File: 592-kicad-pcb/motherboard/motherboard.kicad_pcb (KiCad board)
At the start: 4 copper layers, 151 parts, among them J1 U.FL, J10 Conn_02x06_Odd_Even, J11 Conn_02x06_Odd_Even, J12 Conn_02x06_Odd_Even, J13 Conn_02x06_Odd_Even, J14 USB_B_Micro, J15 Micro_SD_Card, J16 Conn_02x01, J17 Conn_02x01, J18 Conn_02x01, J19 Conn_01x16, J2 U.FL, J20 Conn_02x06_Odd_Even, J21 Conn_02x01, J22 Conn_02x01, J23 Conn_01x16, J24 DF40C-40DP-0.4V(51), J3 DF40C-40DP-0.4V(51), J4 Conn_01x16, J5 2.54mm jumper, J6 U.FL, J7 Conn_02x06_Odd_Even, J8 Conn_02x06_Odd_Even, J9 Conn_02x06_Odd_Even, SW1 C318884, U1 OPA2328DGKR, U10 FT4232H, U11 74HC595, U12 W25Q32JVSS, U13 SN74LVC1G3157DBVR, U14 74CBTLV3257, U15 74CBTLV3257, U16 NUCLEO144-H743ZI, U17 74CBTLV3257, U18 SN74LVC1G14DBV, U19 SN74LVC1G14DBV, U2 74LVC1T45GW, U3 SN74LVC1G14DBV, U4 74LVC1T45GW, U5 SMXS-04K, U6 SX3M10.000B10F20TNN, U7 74LVC1T45GW, U8 SN74LVC1G3157DBVR, U9 SN74LVC1G3157DBVR, Y1 NX3225GA-25.000M-STD-CRG-2, Y2 Si5351A, Y3 X322512MSB4SI

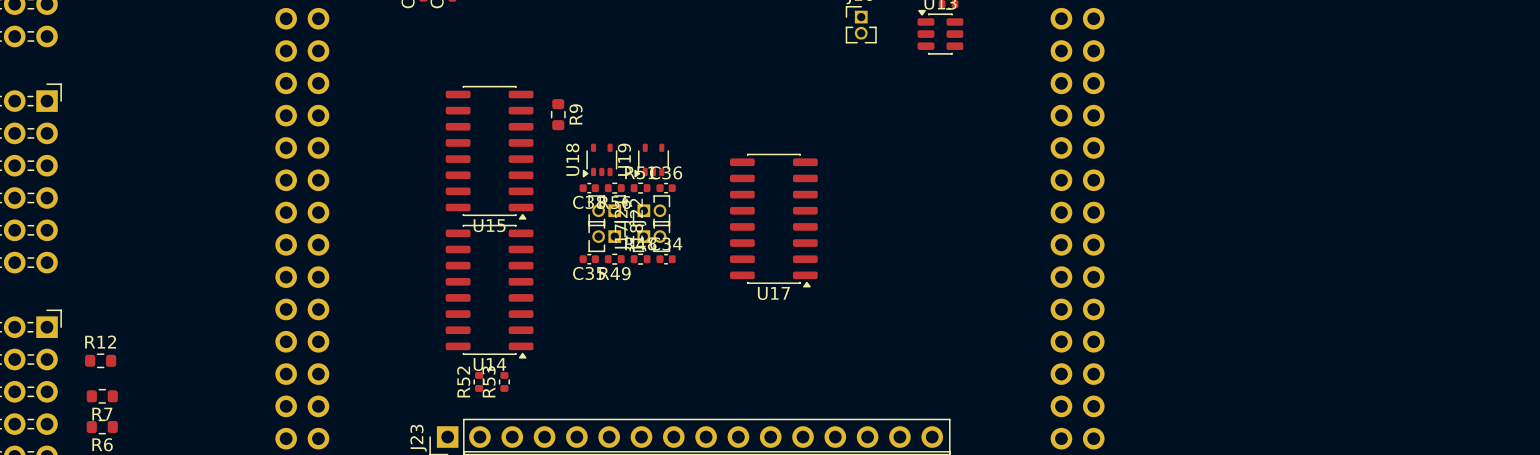
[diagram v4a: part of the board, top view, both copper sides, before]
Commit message: map to STM pins
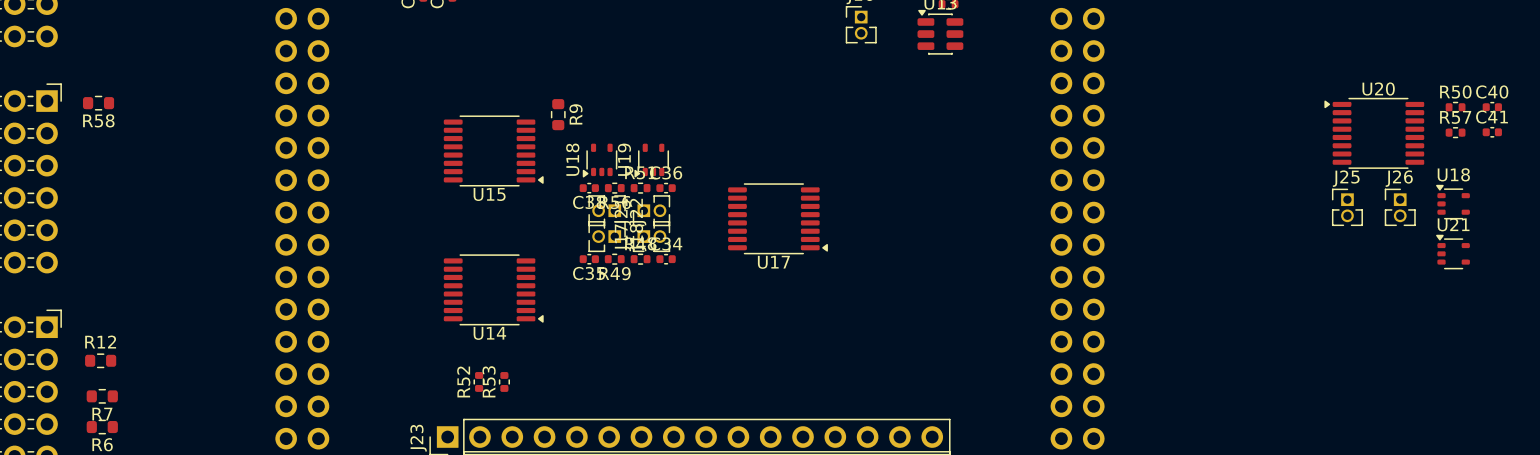
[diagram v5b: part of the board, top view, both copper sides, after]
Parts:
- added C40: 100n, Capacitor_SMD:C_0402_1005Metric, F.Cu at (215.1, 65.8)
- added C41: 100n, Capacitor_SMD:C_0402_1005Metric, F.Cu at (215.1, 67.8)
- added J25: Conn_02x01, Connector_PinHeader_1.27mm:PinHeader_1x02_P1.27mm_Vertical, F.Cu at (203.7, 73.1)
- added J26: Conn_02x01, Connector_PinHeader_1.27mm:PinHeader_1x02_P1.27mm_Vertical, F.Cu at (207.8, 73.1)
- added R50: 10k, Resistor_SMD:R_0402_1005Metric, F.Cu at (212.2, 65.8)
- added R57: 10k, Resistor_SMD:R_0402_1005Metric, F.Cu at (212.2, 67.8)
- added R58: 10k, Resistor_SMD:R_0603_1608Metric, F.Cu at (105.5, 65.5)
- added U18: SN74LVC1G00DCK, Package_TO_SOT_SMD:SOT-353_SC-70-5, F.Cu at (212.1, 73.4)
- added U20: 74CBTLV3257PW,118, Package_SO:TSSOP-16_4.4x5mm_P0.65mm, F.Cu at (206.1, 67.9)
- added U21: SN74LVC1G14DBV, Package_TO_SOT_SMD:SOT-353_SC-70-5, F.Cu at (212.1, 77.3)
- U14, U15, U17: value 74CBTLV3257 -> 74CBTLV3257PW,118; footprint Package_SO:SOIC-16_3.9x9.9mm_P1.27mm -> Package_SO:TSSOP-16_4.4x5mm_P0.65mm

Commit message: updates to routing
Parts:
- added JP3: SolderJumper_2_Bridged, Jumper:SolderJumper-2_P1.3mm_Bridged2Bar_Pad1.0x1.5mm, F.Cu at (-159.7, 59.6)
- added JP4: SolderJumper_2_Bridged, Jumper:SolderJumper-2_P1.3mm_Bridged2Bar_Pad1.0x1.5mm, F.Cu at (-159.7, 63.2)
- added JP5: SolderJumper_2_Bridged, Jumper:SolderJumper-2_P1.3mm_Bridged2Bar_Pad1.0x1.5mm, F.Cu at (-159.7, 66.7)
- moved C14 203.0 mm to (-71.7, 36.4)
- moved C15 203.0 mm to (-66.2, 40.3)
- moved C16 203.0 mm to (-68.1, 40.3)
- moved C18 203.0 mm to (-71.0, 40.6)
- moved C20 203.0 mm to (-73.8, 35.0)
- moved R38 203.0 mm to (-73.8, 33.7)
- moved C19 203.0 mm to (-63.1, 53.5)
- moved C30 203.0 mm to (-59.4, 53.0)
- moved C38 203.0 mm to (12.1, 67.5)
- moved C40 203.0 mm to (12.1, 65.6)
- moved D1 203.0 mm to (-48.2, 53.6)
- moved D2 203.0 mm to (-48.2, 49.8)
- moved D3 203.0 mm to (-48.2, 46.0)
- moved D4 203.0 mm to (-48.2, 42.2)
- moved D5 203.0 mm to (-46.6, 53.6)
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- renumbered C9 to C10, C37 to C11, C10 to C12, C11 to C13, C12 to C14, C13 to C15, C14 to C16, C15 to C17, C16 to C18, C17 to C19, C18 to C20, C19 to C21, C20 to C22, C21 to C23, C22 to C24, C23 to C25, C24 to C26, C25 to C27, C26 to C28, C27 to C29, C28 to C30, C29 to C31, C30 to C32, C31 to C33, C32 to C34, C33 to C35, C38 to C37, C41 to C38, C34 to C39, C35 to C41, C39 to C6, C6 to C7, C7 to C8, C8 to C9, J7 to J10, J8 to J11, J9 to J12, J10 to J13, J11 to J14, J20 to J15, J12 to J16, J13 to J17, J14 to J18, J15 to J19, J16 to J20, J26 to J23, J17 to J24, J18 to J26, J24 to J4, J4 to J5, J19 to J6, J23 to J7, J5 to J8, J6 to J9, R58 to R10, R10 to R11, R11 to R12, R12 to R13, R13 to R14, R14 to R15, R15 to R16, R16 to R17, R17 to R18, R18 to R19, R19 to R20, R20 to R21, R21 to R22, R22 to R23, R23 to R24, R24 to R25, R25 to R26, R26 to R27, R27 to R28, R28 to R29, R29 to R30, R30 to R31, R31 to R32, R32 to R33, R33 to R34, R34 to R35, R35 to R36, R36 to R37, R37 to R38, R38 to R39, R39 to R40, R40 to R41, R41 to R42, R42 to R43, R43 to R44, R44 to R45, R45 to R46, R46 to R47, R54 to R48, R55 to R49, R47 to R50, R56 to R52, R57 to R53, R49 to R54, R48 to R55, R50 to R56, R52 to R57, R53 to R58, U16 to U1, U9 to U10, U10 to U11, U11 to U12, U12 to U13, U13 to U14, U19 to U15, U18 to U16, U14 to U17, U21 to U18, U17 to U19, U1 to U2, U15 to U20, U20 to U21, U2 to U3, U3 to U4, U4 to U5, U5 to U6, U6 to U7, U7 to U8, U8 to U9
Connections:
- J12 pad 2: /motherboard_top/mgmt_debug -> /PG12
- J12 pad 6: /motherboard_top/UART_mgmt_uart_tx -> /PE0_UART8_RX
- J12 pad 8: /motherboard_top/UART_mgmt_uart_rx -> /PE1_UART8_TX
- J3 pad 13: /motherboard_top/chip_connection/user_3v3 -> GND
- J3 pad 2: GND -> /motherboard_top/chip_connection/user_3v3
- J5 pad 1: /motherboard_top/mgmt_debug -> unconnected-(J5-Pin_1-Pad1)
- J5 pad 10: /motherboard_top/chip_connection/MGMT_flash2_sck -> /PE0_UART8_RX
- J5 pad 11: /motherboard_top/chip_connection/MGMT_flash2_io0 -> /PE1_UART8_TX
- J5 pad 12: /motherboard_top/chip_connection/MGMT_flash2_io1 -> /motherboard_top/mgmt_sck
- J5 pad 13: /motherboard_top/chip_connection/MGMT_irq2 -> /motherboard_top/mgmt_csb
- J5 pad 14: unconnected-(J4-Pin_14-Pad14) -> /motherboard_top/mgmt_sdi
- J5 pad 15: unconnected-(J4-Pin_15-Pad15) -> /motherboard_top/mgmt_sdo
- J5 pad 16: unconnected-(J4-Pin_16-Pad16) -> /PG12
- J5 pad 2: /motherboard_top/mgmt_sdo -> unconnected-(J5-Pin_2-Pad2)
- J5 pad 3: /motherboard_top/mgmt_sdi -> unconnected-(J5-Pin_3-Pad3)
- J5 pad 4: /motherboard_top/mgmt_csb -> /PD7
- J5 pad 5: /motherboard_top/mgmt_sck -> /PG1
- J5 pad 6: /motherboard_top/UART_mgmt_uart_rx -> /PG0
- J5 pad 7: /motherboard_top/UART_mgmt_uart_tx -> /PG9
- J5 pad 8: /motherboard_top/chip_connection/MGMT_irq -> /PG15
- J5 pad 9: /motherboard_top/chip_connection/MGMT_flash2_csb -> /PG10
- J6 pad 1: /motherboard_top/chip_connection/mprj_io_0 -> unconnected-(J6-Pin_1-Pad1)
- J6 pad 10: /motherboard_top/chip_connection/mprj_io_9 -> /motherboard_top/chip_connection/mprj_io_6
- J6 pad 11: /motherboard_top/chip_connection/mprj_io_10 -> /motherboard_top/chip_connection/mprj_io_5
- J6 pad 12: /motherboard_top/chip_connection/mprj_io_11 -> /motherboard_top/chip_connection/mprj_io_4
- J6 pad 13: /motherboard_top/chip_connection/mprj_io_12 -> /motherboard_top/chip_connection/mprj_io_3
- J6 pad 14: unconnected-(J19-Pin_14-Pad14) -> /motherboard_top/chip_connection/mprj_io_2
- J6 pad 15: unconnected-(J19-Pin_15-Pad15) -> /motherboard_top/chip_connection/mprj_io_1
- J6 pad 16: unconnected-(J19-Pin_16-Pad16) -> /motherboard_top/chip_connection/mprj_io_0
- J6 pad 2: /motherboard_top/chip_connection/mprj_io_1 -> unconnected-(J6-Pin_2-Pad2)
- J6 pad 3: /motherboard_top/chip_connection/mprj_io_2 -> unconnected-(J6-Pin_3-Pad3)
- J6 pad 4: /motherboard_top/chip_connection/mprj_io_3 -> /motherboard_top/chip_connection/mprj_io_12
- J6 pad 5: /motherboard_top/chip_connection/mprj_io_4 -> /motherboard_top/chip_connection/mprj_io_11
- J6 pad 6: /motherboard_top/chip_connection/mprj_io_5 -> /motherboard_top/chip_connection/mprj_io_10
- J6 pad 7: /motherboard_top/chip_connection/mprj_io_6 -> /motherboard_top/chip_connection/mprj_io_9
- J6 pad 8: /motherboard_top/chip_connection/mprj_io_7 -> /motherboard_top/chip_connection/mprj_io_8
- J6 pad 9: /motherboard_top/chip_connection/mprj_io_8 -> /motherboard_top/chip_connection/mprj_io_7
- J7 pad 1: /motherboard_top/chip_rck_jtag_tck -> unconnected-(J7-Pin_1-Pad1)
- J7 pad 10: /motherboard_top/chip_rck_gpio_0_0 -> /motherboard_top/chip_rck_spi_0_cs_0
- J7 pad 11: /motherboard_top/chip_rck_gpio_1_0 -> /motherboard_top/chip_rck_spi_0_dq_0_mosi
- J7 pad 12: /motherboard_top/chip_rck_i2c_sda -> /motherboard_top/chip_rck_spi_0_dq_1_miso
- J7 pad 13: /motherboard_top/chip_rck_i2c_scl -> /motherboard_top/chip_rck_jtag_tdo
- J7 pad 14: unconnected-(J23-Pin_14-Pad14) -> /motherboard_top/chip_rck_jtag_tdi
- J7 pad 15: unconnected-(J23-Pin_15-Pad15) -> /motherboard_top/chip_rck_jtag_tms
- J7 pad 16: unconnected-(J23-Pin_16-Pad16) -> /motherboard_top/chip_rck_jtag_tck
- J7 pad 2: /motherboard_top/chip_rck_jtag_tms -> unconnected-(J7-Pin_2-Pad2)
- J7 pad 3: /motherboard_top/chip_rck_jtag_tdi -> unconnected-(J7-Pin_3-Pad3)
- J7 pad 4: /motherboard_top/chip_rck_jtag_tdo -> /motherboard_top/chip_rck_i2c_scl
- J7 pad 5: /motherboard_top/chip_rck_spi_0_dq_1_miso -> /motherboard_top/chip_rck_i2c_sda
- J7 pad 6: /motherboard_top/chip_rck_spi_0_dq_0_mosi -> /motherboard_top/chip_rck_gpio_1_0
- J7 pad 7: /motherboard_top/chip_rck_spi_0_cs_0 -> /motherboard_top/chip_rck_gpio_0_0
- J7 pad 8: /motherboard_top/chip_rck_spi_0_sck -> /motherboard_top/GPIO_chip_rck_reset_io
- J7 pad 9: /motherboard_top/GPIO_chip_rck_reset_io -> /motherboard_top/chip_rck_spi_0_sck
- J8 pad 3: /motherboard_top/chip_support_misc/VREF_DAC_OUT -> /PA4_DAC_OUT1
- R25 pad 2: /motherboard_top/clock_sources/fs_ext_gen -> /motherboard_top/clock_sources/ext_clk_dig_gen
- R26 pad 2: /motherboard_top/clock_sources/ext_clk_dig_gen -> /motherboard_top/clock_sources/fs_ext_gen
- R29 pad 2: /motherboard_top/clock_sources/ext_clk_dig_gen -> /motherboard_top/clock_sources/fs_ext_gen
- R31 pad 2: /motherboard_top/clock_sources/fs_ext_gen -> /motherboard_top/clock_sources/ext_clk_dig_gen
- R34 pad 2: /motherboard_top/clock_sources/CLK_DIG_GPIO_GEN -> /PB14_TIM12_CH1
- U1 pad 100: unconnected-(U16-LD3/PB14-Pad100) -> /PB14_TIM12_CH1
- U1 pad 11: unconnected-(U16-PF7-Pad11) -> /PF7_SPI5_SCK
- U1 pad 136: unconnected-(U16-PE0-Pad136) -> /PE0_UART8_RX
- U1 pad 28: unconnected-(U16-PA0-Pad28) -> /PA0_UART4_RX
- U1 pad 30: unconnected-(U16-ETH_REF_CLK/PA1-Pad30) -> /PA1_UART4_TX
- U1 pad 32: unconnected-(U16-PA4-Pad32) -> /PA4_DAC_OUT1
- U1 pad 45: unconnected-(U16-PD7-Pad45) -> /PD7
- U1 pad 54: unconnected-(U16-PF8-Pad54) -> /PF8_SPI5_MISO
- U1 pad 56: unconnected-(U16-PF9-Pad56) -> /PF9_SPI5_MOSI
- U1 pad 58: unconnected-(U16-PG1-Pad58) -> /PG1
- U1 pad 59: unconnected-(U16-PG0-Pad59) -> /PG0
- U1 pad 61: unconnected-(U16-PE1-Pad61) -> /PE1_UART8_TX
- U1 pad 63: unconnected-(U16-PG9-Pad63) -> /PG9
- U1 pad 64: unconnected-(U16-PG15-Pad64) -> /PG15
- U1 pad 65: unconnected-(U16-PG12-Pad65) -> /PG12
- U1 pad 66: unconnected-(U16-PG10-Pad66) -> /PG10
- U1 pad 75: unconnected-(U16-PB8-Pad75) -> /PB8_I2C4_SCL
- U1 pad 77: unconnected-(U16-PB9-Pad77) -> /PB9_I2C4_SDA
- U1 pad 9: unconnected-(U16-PF6-Pad9) -> /PF6_SPI5_CS
- U10 pad 3: /motherboard_top/clock_sources/CLK_DIG_GPIO_GEN -> /PB14_TIM12_CH1
- U11 pad 38: /motherboard_top/UART_mgmt_uart_rx -> /PE1_UART8_TX
- U11 pad 39: /motherboard_top/UART_mgmt_uart_tx -> /PE0_UART8_RX
- U11 pad 48: /motherboard_top/ftdi/ftdi4_uart_tx -> /PA0_UART4_RX
- U11 pad 52: /motherboard_top/ftdi/ftdi4_uart_rx -> /PA1_UART4_TX
- U18 pad 1: unconnected-(U21-NC-Pad1) -> unconnected-(U18-NC-Pad1)
- U19 pad 10: /motherboard_top/GPIO_chip_nfc_jtag_tdo -> /motherboard_top/chip_nfc_jtag_tms
- U19 pad 11: /motherboard_top/chip_rck_jtag_tdo -> /motherboard_top/chip_rck_jtag_tms
- U19 pad 2: /motherboard_top/chip_rck_jtag_tms -> /motherboard_top/chip_rck_jtag_tdo
- U19 pad 3: /motherboard_top/chip_nfc_jtag_tms -> /motherboard_top/GPIO_chip_nfc_jtag_tdo
- U19 pad 4: /motherboard_top/ftdi1_jtag_tms -> /motherboard_top/ftdi1_jtag_tdo
- U19 pad 9: /motherboard_top/ftdi1_jtag_tdo -> /motherboard_top/ftdi1_jtag_tms
- U21 pad 10: /motherboard_top/SPI_MGMT_MOSI -> /PF9_SPI5_MOSI
- U21 pad 13: /motherboard_top/SPI_MGMT_MISO -> /PF8_SPI5_MISO
- U21 pad 3: /motherboard_top/SPI_MGMT_CSb -> /PF6_SPI5_CS
- U21 pad 6: /motherboard_top/SPI_MGMT_SCK -> /PF7_SPI5_SCK
- Y2 pad 4: /motherboard_top/clock_sources/SCL -> /PB8_I2C4_SCL
- Y2 pad 5: /motherboard_top/clock_sources/SDA -> /PB9_I2C4_SDA
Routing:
- net /motherboard_top/chip_nfc_fs: track 0.00 -> 27.2 mm
- net /motherboard_top/chip_nfc_ana_mux_out_2: track 0.00 -> 22.1 mm, vias 0 -> 2
- net /motherboard_top/chip_nfc_ext_clk_dig: track 0.00 -> 18.7 mm
- net +3V3: track 0.00 -> 11.2 mm
- net /motherboard_top/chip_rck_jtag_tdo: track 0.00 -> 9.50 mm
- net GND: track 0.00 -> 9.30 mm, vias 0 -> 2
- net /motherboard_top/chip_rck_jtag_tck: track 0.00 -> 8.85 mm
- net /motherboard_top/chip_rck_jtag_tdi: track 0.00 -> 8.33 mm
- net /motherboard_top/chip_rck_jtag_tms: track 0.00 -> 7.83 mm
- net /PB14_TIM12_CH1: track 0.00 -> 7.71 mm
- net +1V8: track 0.00 -> 6.48 mm
- net Net-(Y2-XA): track 0.00 -> 6.23 mm
- net Net-(Y2-XB): track 0.00 -> 6.23 mm
- net /motherboard_top/clock_sources/EXT_CLK_DIG_SEL: track 0.00 -> 5.08 mm
- net /motherboard_top/clock_sources/CARAVEL_CLK_EN: track 0.00 -> 5.03 mm
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
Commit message: more routing progress, add termination resistors
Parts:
- moved R1 275.4 mm to (176.7, 108.6)
- moved U3 275.3 mm to (174.4, 109.2)
- moved R23 13.1 mm to (188.0, 105.5), turned to 180 degrees
- moved C8 12.4 mm to (188.0, 104.4), turned to 0 degrees
- moved R24 11.7 mm to (188.0, 103.0), turned to 180 degrees
- moved C10 11.3 mm to (188.0, 101.9), turned to 0 degrees
- moved C12 11.3 mm to (188.0, 99.4), turned to 0 degrees
- moved R30 11.2 mm to (188.0, 100.5), turned to 180 degrees
- moved U6 1.62 mm to (194.9, 101.2), turned to 90 degrees
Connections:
- C10 pad 2: /motherboard_top/clock_sources/CARAVEL_CLK_EN -> /motherboard_top/clock_sources/FS_EXT_SEL
- C12 pad 2: /motherboard_top/clock_sources/FS_EXT_SEL -> /motherboard_top/clock_sources/CARAVEL_CLK_EN
- R24 pad 1: /motherboard_top/clock_sources/CARAVEL_CLK_EN -> /motherboard_top/clock_sources/FS_EXT_SEL
- R30 pad 1: /motherboard_top/clock_sources/FS_EXT_SEL -> /motherboard_top/clock_sources/CARAVEL_CLK_EN
- U6 pad 6: /motherboard_top/clock_sources/FS_EXT_SEL -> /motherboard_top/clock_sources/CARAVEL_CLK_EN
- U6 pad 7: /motherboard_top/clock_sources/CARAVEL_CLK_EN -> /motherboard_top/clock_sources/FS_EXT_SEL
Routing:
- net /motherboard_top/chip_rck_clock_uncore: track 4.40 -> 34.2 mm
- net /motherboard_top/chip_nfc_ana_mux_out: track 0.00 -> 24.0 mm, vias 0 -> 2
- net /motherboard_top/clock_sources/FS_EXT_SEL: track 5.01 -> 27.6 mm, vias 0 -> 2
- net /motherboard_top/clock_sources/CARAVEL_CLK_EN: track 5.03 -> 24.9 mm
- net /motherboard_top/clock_sources/EXT_CLK_DIG_SEL: track 5.08 -> 22.8 mm, vias 0 -> 2
- net /motherboard_top/chip_nfc_nfc_afe_tdo: track 1.06 -> 6.32 mm
- net /motherboard_top/chip_connection/user_3v3: track 0.00 -> 3.39 mm, vias 0 -> 2
- net /motherboard_top/chip_connection/mprj_io_7: track 0.00 -> 2.72 mm, vias 0 -> 1
- net /motherboard_top/chip_connection/mprj_io_12: track 0.00 -> 2.44 mm, vias 0 -> 1
- net /motherboard_top/chip_connection/mprj_io_6: track 0.00 -> 2.31 mm, vias 0 -> 1
- net /motherboard_top/chip_connection/mprj_io_8: track 0.00 -> 2.20 mm, vias 0 -> 1
- net /motherboard_top/chip_connection/mprj_io_11: track 0.00 -> 2.19 mm, vias 0 -> 1
- net /motherboard_top/GPIO_chip_nfc_jtag_tdo2: track 0.00 -> 1.87 mm, vias 0 -> 1
- net /motherboard_top/chip_connection/mprj_io_5: track 0.00 -> 1.81 mm, vias 0 -> 1
- net /motherboard_top/chip_connection/mprj_io_9: track 0.00 -> 1.77 mm, vias 0 -> 1
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
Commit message: core routing progress
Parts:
- removed J5, J6, J7: Conn_01x16, Connector_PinHeader_2.54mm:PinHeader_1x16_P2.54mm_Vertical
- removed R15, R16, R17, R20: 10k, Resistor_SMD:R_0603_1608Metric
- removed the U18 at (-57.9, 69.7)
- added C48: 0, Capacitor_SMD:C_0402_1005Metric, F.Cu at (164.9, 96.0)
- added C49: 0, Capacitor_SMD:C_0402_1005Metric, F.Cu at (161.4, 94.1)
- added C50: 100n, Capacitor_SMD:C_0402_1005Metric, F.Cu at (105.3, 106.9)
- added C51: 100p, Capacitor_SMD:C_0402_1005Metric, F.Cu at (70.9, 29.2)
- added C52: 100p, Capacitor_SMD:C_0402_1005Metric, F.Cu at (70.9, 31.2)
- added C53: 10n, Capacitor_SMD:C_0402_1005Metric, F.Cu at (70.9, 33.2)
- added D10: SMAJ10CA, Diode_SMD:D_SMA, F.Cu at (83.2, 33.1)
- added D11: SMAJ10CA, Diode_SMD:D_SMA, F.Cu at (83.2, 37.6)
- added D9: SMAJ10CA, Diode_SMD:D_SMA, F.Cu at (83.2, 28.6)
- added J31: Conn_02x01, Connector_PinHeader_1.27mm:PinHeader_1x02_P1.27mm_Vertical, F.Cu at (107.3, 108.7)
- added R100: 0, Resistor_SMD:R_0402_1005Metric, F.Cu at (172.5, 100.6)
- added R101: 0, Resistor_SMD:R_0402_1005Metric, F.Cu at (172.0, 101.8)
- added R102: 0, Resistor_SMD:R_0402_1005Metric, F.Cu at (172.4, 103.0)
- added R103: 0, Resistor_SMD:R_0402_1005Metric, F.Cu at (172.4, 104.2)
- added R64: 0, Resistor_SMD:R_0402_1005Metric, F.Cu at (77.6, 27.3)
- added R65: 0, Resistor_SMD:R_0402_1005Metric, F.Cu at (77.6, 29.3)
- added R66: 27, Resistor_SMD:R_0402_1005Metric, F.Cu at (82.5, 49.2)
- added R67: 10k, Resistor_SMD:R_0402_1005Metric, F.Cu at (82.5, 51.2)
- added R68: 2k, Resistor_SMD:R_0603_1608Metric, F.Cu at (58.3, 55.9)
- added R69: 2k, Resistor_SMD:R_0603_1608Metric, F.Cu at (58.3, 58.4)
- added R70: 0, Resistor_SMD:R_0402_1005Metric, F.Cu at (163.5, 107.2)
- added R71: 10k, Resistor_SMD:R_0402_1005Metric, F.Cu at (77.6, 45.2)
- added R72: 10k, Resistor_SMD:R_0402_1005Metric, F.Cu at (77.6, 47.2)
- added R73: 10k, Resistor_SMD:R_0603_1608Metric, F.Cu at (67.5, 27.5)
- added R78: 100, Resistor_SMD:R_0402_1005Metric, F.Cu at (157.9, 97.9)
- added R79: 100, Resistor_SMD:R_0402_1005Metric, F.Cu at (163.2, 101.1)
- added R80: 100, Resistor_SMD:R_0402_1005Metric, F.Cu at (174.4, 111.2)
- added R84: 75, Resistor_SMD:R_0603_1608Metric, F.Cu at (67.5, 30.0)
- added R86: 75, Resistor_SMD:R_0603_1608Metric, F.Cu at (67.5, 32.5)
- added R87: 0, Resistor_SMD:R_0402_1005Metric, F.Cu at (141.8, 93.7)
- added R88: 0, Resistor_SMD:R_0402_1005Metric, F.Cu at (173.3, 105.8)
- added R89: 0, Resistor_SMD:R_0402_1005Metric, F.Cu at (148.0, 104.5)
- added R90: 10k, Resistor_SMD:R_0603_1608Metric, F.Cu at (67.5, 35.1)
- added R91: 10k, Resistor_SMD:R_0603_1608Metric, F.Cu at (67.5, 37.6)
- added R92: 10k, Resistor_SMD:R_0402_1005Metric, F.Cu at (77.6, 31.2)
- added R93: 22, Resistor_SMD:R_0402_1005Metric, F.Cu at (77.6, 33.2)
- added R94: 22, Resistor_SMD:R_0402_1005Metric, F.Cu at (77.6, 35.2)
- added R95: 22, Resistor_SMD:R_0402_1005Metric, F.Cu at (77.6, 37.2)
- added R96: 22, Resistor_SMD:R_0402_1005Metric, F.Cu at (77.6, 39.2)
- added R97: 22, Resistor_SMD:R_0402_1005Metric, F.Cu at (77.6, 41.2)
- added R98: 10k, Resistor_SMD:R_0402_1005Metric, F.Cu at (77.6, 49.2)
- added R99: 10k, Resistor_SMD:R_0402_1005Metric, F.Cu at (77.6, 51.2)
- added U29: 74CBTLV3257PW,118, Package_SO:TSSOP-16_4.4x5mm_P0.65mm, F.Cu at (151.6, 98.3)
- added U30: 74CBTLV3257PW,118, Package_SO:TSSOP-16_4.4x5mm_P0.65mm, F.Cu at (151.6, 91.8)
- added U31: 74CBTLV3257PW,118, Package_SO:TSSOP-16_4.4x5mm_P0.65mm, F.Cu at (136.7, 91.7)
- added U32: 74CBTLV3257PW,118, Package_SO:TSSOP-16_4.4x5mm_P0.65mm, F.Cu at (136.7, 98.2)
- R10, R14, R18, R19, R8, R9: footprint Resistor_SMD:R_0603_1608Metric -> Resistor_SMD:R_0402_1005Metric
- R48, R49: value 10k -> 100k
- U1: moved to F.Cu
- moved R18 202.0 mm to (103.7, 109.9), turned to 0 degrees
- moved R14 187.1 mm to (66.9, 45.8), turned to 0 degrees
- moved R19 186.5 mm to (69.8, 39.8)
- moved R8 175.5 mm to (66.9, 39.8), turned to 0 degrees
- moved R10 165.8 mm to (66.9, 43.8), turned to 0 degrees
- moved R48 139.3 mm to (82.5, 45.2), turned to 0 degrees
- moved R9 130.5 mm to (66.9, 41.8), turned to 0 degrees
- moved R49 129.5 mm to (82.5, 47.2), turned to 0 degrees
- moved U1 67.6 mm to (-85.8, 46.8), turned to 0 degrees
- moved U16 42.5 mm to (194.8, 130.8)
- moved U15 26.4 mm to (164.0, 110.3), turned to 180 degrees
- moved U19 23.3 mm to (157.1, 110.5), turned to 0 degrees
- moved C1 1.69 mm to (160.7, 96.1)
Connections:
- C38 pad 1: /motherboard_top/GPIO_SPI_MGMT_enable -> /motherboard_top/GPIO_MGMT_enable
- J19 pad 7: /motherboard_top/rck_mem_miso_i01 -> Net-(J19-DAT0)
- J23 pad 2: /motherboard_top/GPIO_SPI_MGMT_enable -> /motherboard_top/GPIO_MGMT_enable
- J3 pad 30: /motherboard_top/GPIO_chip_nfc_jtag_tdo2 -> Net-(J3-Pad30)
- J4 pad 11: /motherboard_top/chip_spi_flash_0_dq_2 -> Net-(J4-Pad11)
- J4 pad 13: /motherboard_top/chip_spi_flash_0_dq_1 -> Net-(J4-Pad13)
- J4 pad 15: /motherboard_top/chip_spi_flash_0_dq_0 -> Net-(J4-Pad15)
- J4 pad 25: /motherboard_top/GPIO_chip_nfc_jtag_tdo -> Net-(J4-Pad25)
- J4 pad 9: /motherboard_top/chip_spi_flash_0_dq_3 -> Net-(J4-Pad9)
- R10 pad 2: /motherboard_top/mgmt_csb -> /motherboard_top/chip_nfc_jtag_tdi
- R11 pad 2: /motherboard_top/chip_connection/resetb -> /motherboard_top/GPIO_chip_nfc_ext_reset_dig
- R14 pad 2: /motherboard_top/chip_nfc_jtag_tms -> /motherboard_top/chip_rck_jtag_tdi
- R18 pad 2: /motherboard_top/chip_rck_jtag_tms -> /motherboard_top/GPIO_MGMT_enable
- R19 pad 1: /motherboard_top/chip_rck_jtag_tdi -> /motherboard_top/chip_nfc_jtag_trst
- R34 pad 2: /PB14_TIM12_CH1 -> Net-(U10-B1)
- R53 pad 2: /motherboard_top/GPIO_SPI_MGMT_enable -> /motherboard_top/GPIO_MGMT_enable
- R8 pad 2: /motherboard_top/chip_rck_spi_0_cs_0 -> /motherboard_top/chip_nfc_jtag_tms
- R9 pad 2: /motherboard_top/chip_spi_flash_0_cs_0 -> /motherboard_top/chip_rck_jtag_tms
- U10 pad 3: /PB14_TIM12_CH1 -> Net-(U10-B1)
- U11 pad 16: /motherboard_top/ftdi1_jtag_tck -> Net-(U11-ADBUS0)
- U11 pad 17: /motherboard_top/ftdi1_jtag_tdi -> Net-(U11-ADBUS1)
- U11 pad 19: /motherboard_top/ftdi1_jtag_tms -> Net-(U11-ADBUS3)
- U11 pad 26: /motherboard_top/ftdi_spi_sck -> Net-(U11-BDBUS0)
- U11 pad 27: /motherboard_top/ftdi_spi_mosi -> Net-(U11-BDBUS1)
- U11 pad 7: /motherboard_top/ftdi/USB_DM -> Net-(U11-DM)
- U11 pad 8: /motherboard_top/ftdi/USB_DP -> Net-(U11-DP)
- U18 pad 2: /motherboard_top/GPIO_SPI_MGMT_enable -> /motherboard_top/GPIO_MGMT_enable
- U19 pad 10: /motherboard_top/chip_nfc_jtag_tms -> /motherboard_top/GPIO_chip_nfc_jtag_tdo
- U19 pad 11: /motherboard_top/chip_rck_jtag_tms -> /motherboard_top/chip_rck_jtag_tdo
- U19 pad 2: /motherboard_top/chip_rck_jtag_tdo -> /motherboard_top/chip_rck_jtag_tms
- U19 pad 3: /motherboard_top/GPIO_chip_nfc_jtag_tdo -> /motherboard_top/chip_nfc_jtag_tms
- U19 pad 4: /motherboard_top/ftdi1_jtag_tdo -> /motherboard_top/ftdi1_jtag_tms
- U19 pad 9: /motherboard_top/ftdi1_jtag_tms -> /motherboard_top/ftdi1_jtag_tdo
- U2 pad 1: /motherboard_top/ADC_chip_ana_mux_out_1 -> /motherboard_top/ana_buffers/a1
- U2 pad 2: /motherboard_top/ADC_chip_ana_mux_out_1 -> /motherboard_top/ana_buffers/a1
- U2 pad 6: /motherboard_top/ADC_chip_ana_mux_out_2 -> /motherboard_top/ana_buffers/a2
- U2 pad 7: /motherboard_top/ADC_chip_ana_mux_out_2 -> /motherboard_top/ana_buffers/a2
- U3 pad 3: /motherboard_top/GPIO_chip_nfc_afe_tdo_ext -> Net-(U3-A)
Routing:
- net Net-(U29E-~{OE}): track 0.00 -> 40.8 mm
- net /motherboard_top/GPIO_MGMT_enable: track 0.00 -> 35.2 mm
- net /motherboard_top/chip_nfc_jtag_tdi: track 2.52 -> 33.6 mm, vias 1 -> 2
- net /motherboard_top/chip_nfc_jtag_tms: track 2.98 -> 30.1 mm, vias 1 -> 2
- net /motherboard_top/clock_sources/fs_ext_aux: track 4.80 -> 26.0 mm
- net /motherboard_top/chip_connection/mprj_io_12: track 2.44 -> 23.5 mm, vias 1 -> 0
- net /motherboard_top/chip_connection/mprj_io_1: track 1.65 -> 20.5 mm, vias 1 -> 2
- net /motherboard_top/chip_connection/mprj_io_11: track 2.19 -> 20.4 mm, vias 1 -> 0
- net /motherboard_top/chip_nfc_jtag_tck: track 2.57 -> 19.1 mm, vias 1 -> 2
- net /motherboard_top/chip_connection/mprj_io_2: track 1.54 -> 17.5 mm, vias 1 -> 2
- net /motherboard_top/GPIO_chip_nfc_jtag_tdo: track 1.97 -> 17.4 mm
- net /motherboard_top/chip_connection/mprj_io_10: track 1.33 -> 14.9 mm, vias 1 -> 0
- net /motherboard_top/chip_connection/mprj_io_4: track 1.29 -> 13.9 mm, vias 1 -> 0
- net /motherboard_top/chip_nfc_ana_mux_out_2: track 23.2 -> 32.7 mm
- net /motherboard_top/chip_connection/mprj_io_5: track 1.81 -> 10.7 mm, vias 1 -> 0
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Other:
- board text added: ":)"
- board text added: "bogos binted?"
